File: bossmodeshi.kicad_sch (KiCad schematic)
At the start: 102 parts, among them Q1 FZT853TA, Q2 PSMN3R7-100BSE, Q3 PSMN3R7-100BSE, Q4 PSMN3R7-100BSE, Q5 PSMN3R7-100BSE, U10 SQ1464EEH-T1_GE3, U11 MP2790DFP-0000-T, U5 SQ1464EEH-T1_GE3, U6 SQ1464EEH-T1_GE3, U7 SQ1464EEH-T1_GE3, U8 SQ1464EEH-T1_GE3, U9 SQ1464EEH-T1_GE3

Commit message: Pushing
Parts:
- added D12, D18, D19, D20, D21, D22, D25: LED, symbol Device:LED
- added NT1: NetTie_2, NetTie:NetTie-2_SMD_Pad2.0mm, symbol Device:NetTie_2
- added R28, R29, R30, R31, R32, R33, R38: R, symbol Device:R
- R19: now fitted
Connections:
- net C1: now also R_BAL_6.1, R33.1; no longer R_BAL_6.2
- net C2: now also R_BAL_5.1, R32.1; no longer R_BAL_5.2
- net C3: now also R_BAL_4.1, R31.1; no longer R_BAL_4.2
- net C4: now also R_BAL_3.1, R30.1; no longer R_BAL_3.2
- net C5: now also R_BAL_2.1, R29.1; no longer R_BAL_2.2
- net GND: now also D25.1 (K), NT1.1; no longer D9.2 (A), DAGND_CO1.2 (A), R_CELL_FLT7.2, R_SENSE1.1, R_SRP_FLT1.1, U10.4 (S)
- net INT_5V: now also R38.2
- net TOP: now also R28.1
- net at U10.1 (D), U10.2 (D), U10.5 (D)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: now also R_BAL_6.2, D22.1 (K); no longer R_BAL_6.1
- net at U9.1 (D), U9.2 (D), U9.5 (D)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: now also R_BAL_5.2, D21.1 (K); no longer R_BAL_5.1
- net at U8.1 (D), U8.2 (D), U8.5 (D)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: now also R_BAL_4.2, D20.1 (K); no longer R_BAL_4.1
- net at U6.1 (D), U6.2 (D), U6.5 (D)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: now also R_BAL_2.2, D18.1 (K); no longer R_BAL_2.1
- net at U7.1 (D), U7.2 (D), U7.5 (D)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: now also R_BAL_3.2, D19.1 (K); no longer R_BAL_3.1
- net at R_BAL_1.1, U5.1 (D), U5.2 (D)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: now also D12.1 (K)
- new net: D20.2 (A), R31.2
- new net: D22.2 (A), R33.2
- new net: D21.2 (A), R32.2
- new net: D18.2 (A), R29.2
- new net: D25.2 (A), R38.1
- new net: D19.2 (A), R30.2
- new net: D12.2 (A), R28.2
- new net BATT-: D9.2 (A), DAGND_CO1.2 (A), NT1.2, R_CELL_FLT7.2, R_SENSE1.1, R_SRP_FLT1.1, U10.4 (S)
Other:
- note added: "One NTC to measure drain node."
- moved on the sheet: C19, C20, C21, C22, C23, C_3V3_1, C_CELL_FLT1, C_CELL_FLT2, C_CELL_FLT3, C_CELL_FLT4, C_CELL_FLT5, C_CELL_FLT6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

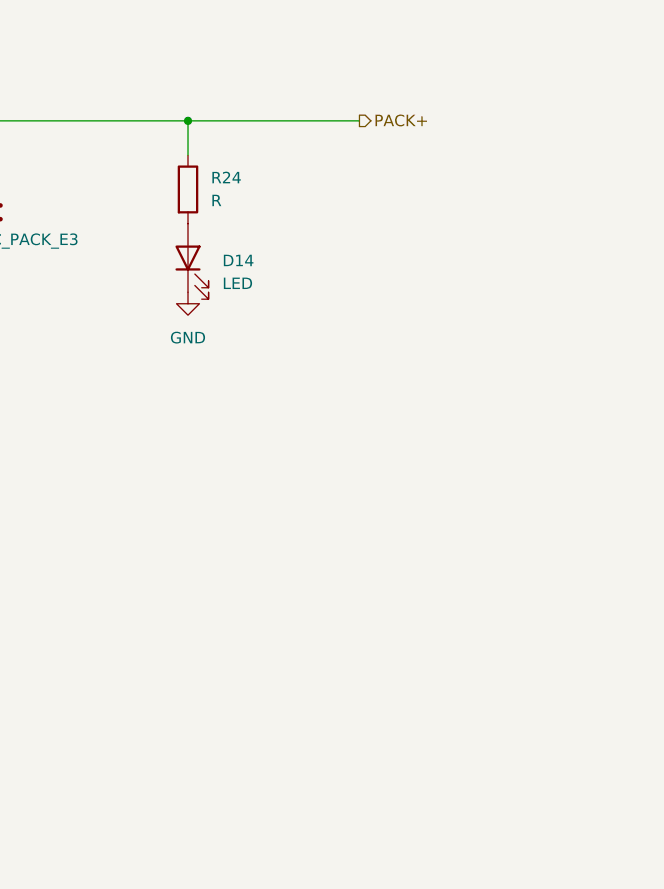
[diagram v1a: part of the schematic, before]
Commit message: reverse polarity protection
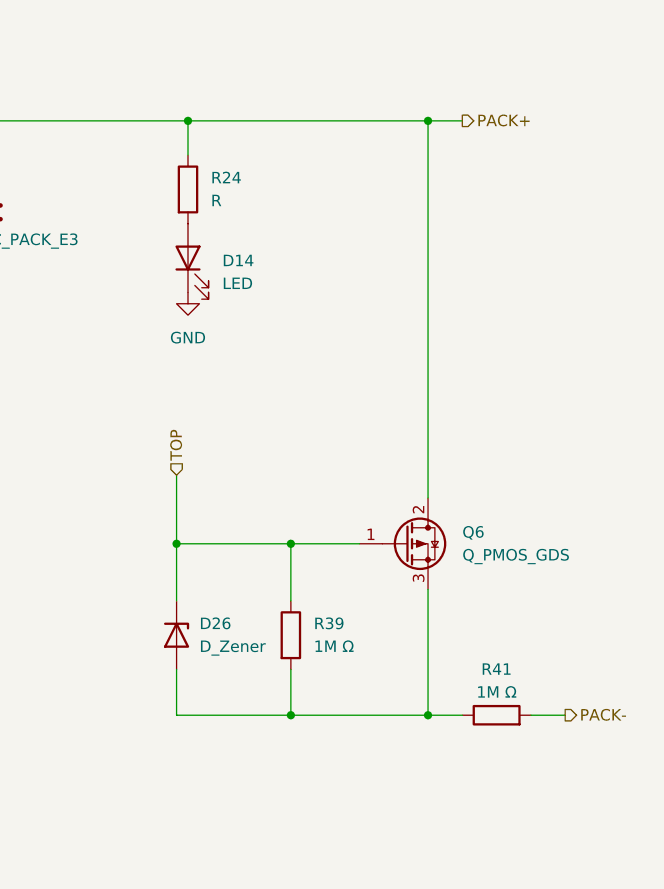
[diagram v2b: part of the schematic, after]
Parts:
- added D26: D_Zener, symbol Device:D_Zener
- added Q6: Q_PMOS_GDS, Package_TO_SOT_SMD:TO-252-2, symbol Transistor_FET:Q_PMOS_GDS
- added R39, R41: 1M Ω, Resistor_SMD:R_0201_0603Metric, symbol Device:R
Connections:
- net PACK+: now also Q6.2 (D)
- net PACK-: now also R41.2
- net TOP: now also D26.1 (K), Q6.1 (G), R39.1
- new net: D26.2 (A), Q6.3 (S), R39.2, R41.1

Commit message: Adding in signals and cleaning up schematic
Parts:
- removed D18, D19, D20, D21, D25: LED, symbol Device:LED
- removed R23: R, Resistor_SMD:R_0603_1608Metric, symbol Device:R
- removed R30, R31, R32, R33, R38: R, symbol Device:R
- added D11, D12, D15, D24, D27: LED, LED_SMD:LED_0603_1608Metric, symbol Device:LED
- added R25, R26, R27, R28, R37, R39: R, Resistor_SMD:R_0603_1608Metric, symbol Device:R
- added R42, R43, R44, R45, R46, R47, R48, R49: R, symbol Device:R
- D10: renamed from D12; footprint (none) -> LED_SMD:LED_0603_1608Metric
- D22: footprint (none) -> LED_SMD:LED_0603_1608Metric
- D26: value D_Zener -> TPSMF4L16A; footprint (none) -> Diode_SMD:Nexperia_CFP3_SOD-123W; Mfr (none) -> Littelfuse Inc.; Mfr P/N (none) -> TPSMF4L16A; Supplier_1 (none) -> Digikey; Supplier_1 P/N (none) -> F7539TR-ND; Supplier_1 Price @ QTY (none) -> 1; Supplier_1 Unit Price (none) -> 0.15000
- Q6: footprint Package_TO_SOT_SMD:TO-252-2 -> _BMS:SOT-23; Mfr P/N (none) -> SI01P10-TP; Mfr PN IRFR9110TRPBF -> (none); Supplier JLCPCB -> (none); Supplier PN C143721 -> (none); Supplier_2 (none) -> JLCPCB; Supplier_2 P/N (none) -> C5917586; Supplier_2 Price @ Qty (none) -> 1; Supplier_2 Unit Price (none) -> 0.0751
- R23: renamed from R28; footprint (none) -> Resistor_SMD:R_0603_1608Metric
- R29: footprint (none) -> Resistor_SMD:R_0603_1608Metric
- R40: renamed from R39; value 1M Ω -> 1MΩ; Mfr P/N (none) -> RC0603FR-071ML; Mfr PN RC0603FR-071ML -> (none); Supplier_2 (none) -> JLCPCB
- R41: value 1M Ω -> 1MΩ; Mfr P/N (none) -> RC0603FR-071ML; Mfr PN RC0603FR-071ML -> (none); Supplier_2 (none) -> JLCPCB
- renumbered C19 to C20, C20 to C21, C21 to C22, C22 to C23, C23 to C24, D4 to D16, D5 to D17, D6 to D18, D7 to D19, D8 to D20, D9 to D21, D10 to D23, D11 to D25, R14 to R30, R15 to R31, R16 to R32, R17 to R33, R18 to R34, R19 to R35, R20 to R36, R21 to R38, U9 to U10, U10 to U11, U11 to U12, U5 to U6, U6 to U7, U7 to U8, U8 to U9
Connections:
- net C1: now also R28.1
- net C2: now also R27.1
- net C3: now also R26.1
- net C4: now also R25.1
- net C5: now also R24.1; no longer R29.1
- net GND: now also D22.1 (K), D24.1 (K), D27.1 (K), R43.2, R45.2, R47.2, R49.2; no longer D13.1 (K), D14.1 (K)
- net INT_5V: now also R37.1
- net PACK+: now also R39.1, R42.1; no longer R24.1
- net TOP: now also R29.1, R44.1; no longer D26.1 (K), Q6.1 (G), R40.1
- net CHG_M: now reaches D_CHG_VGS1.1 (K), R_CHG_DRIVER1.2, R_CHG_MG1.2, R_CHG_MG2.1, R_CHG_PUP1.2
- net CHG_M: now also R48.1
- net at D26.2 (A), R40.2, R41.1: now also Q6.1 (G); no longer Q6.3 (S)
- net at R_BAL_6.2, U11.1 (D), U11.2 (D)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: now also D15.1 (K); no longer D22.1 (K)
- net DSG_M: now reaches D_CHG_VGS2.1 (K), R_DSG_DRIVER1.1, R_DSG_MG1.2, R_DSG_MG2.1, R_DSG_PUP1.1
- net DSG_M: now also R46.1
- net at R_BAL_5.2, U10.1 (D), U10.2 (D)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: now also D14.1 (K)
- net at D22.2 (A): now also R29.2
- net at R_BAL_4.2, U9.1 (D), U9.2 (D)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: now also D13.1 (K)
- net at R_BAL_2.2, U7.1 (D), U7.2 (D)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: now also D11.1 (K)
- net at R_BAL_3.2, U8.1 (D), U8.2 (D)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: now also D12.1 (K)
- net at D13.2 (A): now also R26.2
- net at R24.2: now also D11.2 (A); no longer D14.2 (A)
- new net: D24.2 (A), R37.2
- new net: D15.2 (A), R28.2
- new net: D14.2 (A), R27.2
- new net: D27.2 (A), R39.2
- new net: D12.2 (A), R25.2
- new net CHG_MV: R48.2, R49.1
- new net DSG_MV: R46.2, R47.1
- new net PACKV: R42.2, R43.1
- new net PACK_F: D26.1 (K), Q6.3 (S), R40.1
- new net TOPV: R44.2, R45.1
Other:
- note added: "Pack voltage divider"
- note added: "Reverse polarity protection"
- note added: "Signals & Comms"
- moved on the sheet: Q6, R40

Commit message: Redoing layout
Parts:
- removed D10, D11, D12, D13, D14, D15: LED, LED_SMD:LED_0603_1608Metric, symbol Device:LED
- removed R23, R24, R25, R26, R27, R28: R, Resistor_SMD:R_0603_1608Metric, symbol Device:R
- R40, R41: footprint Resistor_SMD:R_0201_0603Metric -> Resistor_SMD:R_0603_1608Metric
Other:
- moved on the sheet: R_BAL_1, R_BAL_2, R_BAL_3, R_BAL_4, R_BAL_5, R_BAL_6

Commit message: prepaing for production
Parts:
- added R36, R37, R38, R39, R40, R41: 10k, Resistor_SMD:R_0603_1608Metric, symbol Device:R
- added TP11, TP12, TP13, TP14: TestPoint, _BMS:Harwin TP, symbol Connector:TestPoint
- C_3V3_1, C_REG1, C_VDD1: Supplier_2 (none) -> JLCPCB; Supplier_2 P/N (none) -> C22443289
- C_CP1: Mfr P/N CC0402JRX7R9BB473 -> CC0603JRX7R9BB473; Supplier_1 DigiKey -> (none); Supplier_1 P/N 13-CC0402JRX7R9BB473TR-ND -> (none); Supplier_1 Price @ QTY 1 -> (none); Supplier_1 Unit Price 0.10000 -> (none); Supplier_2 (none) -> JLCPCB; Supplier_2 P/N (none) -> C519554
- C_MID1: Mfr Murata Electronics -> YAGEO; Mfr P/N GRM155C71H104JE19D -> CC0603JRX7R9BB104; Supplier_1 DigiKey -> (none); Supplier_1 P/N 490-GRM155C71H104JE19DTR-ND -> (none); Supplier_1 Price @ QTY 1 -> (none); Supplier_1 Unit Price 0.10000 -> (none); Supplier_2 (none) -> JLCPCB; Supplier_2 P/N (none) -> C91183
- C_PACK_E1, C_PACK_E2: now left out of the parts list
- C_PACK_E3: now not fitted; now left out of the parts list
- C_REGIN1: Mfr Cal-Chip Electronics, Inc. -> TDK; Mfr P/N GMC10X5R335K25NT -> C1608X5R1E335KT000E; Supplier_1 DigiKey -> (none); Supplier_1 P/N 4713-GMC10X5R335K25NTTR-ND -> (none); Supplier_1 Price @ QTY 0.41000 -> (none); Supplier_1 Unit Price 1 -> (none); Supplier_2 (none) -> JLCPCB; Supplier_2 P/N (none) -> C342962
- C_TOP_FLT1: Mfr TDK Corporation -> YAGEO; Mfr P/N CGA3E3X7R1H474K080AE -> CC0603KRX7R9BB474; Supplier_1 Digikey -> (none); Supplier_1 P/N 445-172475-2-ND -> (none); Supplier_1 Price @ QTY 1 -> (none); Supplier_1 Unit Price 0.31000 -> (none); Supplier_2 (none) -> JLCPCB; Supplier_2 P/N (none) -> C513577; Supplier_2 Price @ QTY (none) -> 0.0105; Supplier_2 Unit Price (none) -> 1
- C_VREF1: Supplier_2 (none) -> JLCPCB; Supplier_2 P/N (none) -> C22443289; Supplier_2 Price @ QTY (none) -> 1; Supplier_2 Unit Price (none) -> 0.0703
- D10: renamed from D16; Supplier_2 (none) -> JLCPCB; Supplier_2 P/N (none) -> C478011
- D11: renamed from D17; Supplier_2 (none) -> JLCPCB; Supplier_2 P/N (none) -> C478011
- D12: renamed from D18; Supplier_2 (none) -> JLCPCB; Supplier_2 P/N (none) -> C478011
- D13: renamed from D19; Supplier_2 (none) -> JLCPCB; Supplier_2 P/N (none) -> C478011
- D14: renamed from D20; Supplier_2 (none) -> JLCPCB; Supplier_2 P/N (none) -> C478011
- D15: renamed from D21; Supplier_2 (none) -> JLCPCB; Supplier_2 P/N (none) -> C478011
- D16: renamed from D22; Mfr (none) -> ROHM Semicon; Mfr P/N (none) -> SML-310LTT86; Supplier_2 (none) -> JLCPCB; Supplier_2 P/N (none) -> C79636
- D17: renamed from D23; Supplier_2 (none) -> JLCPCB
- D18: renamed from D24; Mfr (none) -> ROHM Semicon; Mfr P/N (none) -> SML-E12P8WT86; Supplier_2 (none) -> JLCPCB; Supplier_2 P/N (none) -> C126319
- D19: renamed from D25; Supplier_2 (none) -> JLCPCB; Supplier_2 P/N (none) -> C5557780
- D20: renamed from D26; Supplier_2 (none) -> JLCPCB; Supplier_2 P/N (none) -> C468927
- D21: renamed from D27; Mfr (none) -> ROHM Semicon; Mfr P/N (none) -> SML-310LTT86; Supplier_2 (none) -> JLCPCB; Supplier_2 P/N (none) -> C79636
- DAGND_CO1: Supplier_2 (none) -> JLCPCB; Supplier_2 P/N (none) -> C150503
- D_CHG_VGS1, D_CHG_VGS2: Supplier_2 (none) -> JLCPCB; Supplier_2 P/N (none) -> C468927
- Q1: Supplier_2 (none) -> JLCPCB; Supplier_2 P/N (none) -> C435890
- Q2, Q3, Q4, Q5: Supplier_2 (none) -> JLCPCB; Supplier_2 P/N (none) -> C406802
- R23: renamed from R29; value R -> 10k; Mfr (none) -> YAGEO; Mfr P/N (none) -> RC0603FR-0710KL; Supplier_2 (none) -> JLCPCB; Supplier_2 P/N (none) -> C98220
- R26: renamed from R32; now left out of the parts list
- R27: renamed from R33; now left out of the parts list
- R28: renamed from R34; now left out of the parts list
- R29: renamed from R35; symbol Device:R -> Device:Thermistor_NTC; Mfr (none) -> Vishay Intertech; Mfr P/N (none) -> NTCS0603E3103FLT; Supplier_2 (none) -> JLCPCB; Supplier_2 P/N (none) -> C142556
- R31: renamed from R37; Mfr (none) -> Yageo; Mfr P/N (none) -> AC0603FR-071KL; Supplier_2 (none) -> JLCPCB; Supplier_2 P/N (none) -> C116692
- R33: renamed from R40; Supplier_2 P/N (none) -> C105578
- R34: renamed from R39; value R -> 10k; Mfr (none) -> YAGEO; Mfr P/N (none) -> RC0603FR-0710KL; Supplier_2 (none) -> JLCPCB; Supplier_2 P/N (none) -> C98220
- R35: renamed from R41; Supplier_2 P/N (none) -> C105578
- R42, R43: value R -> 10k; footprint (none) -> Resistor_SMD:R_0603_1608Metric; Mfr (none) -> Yageo; Mfr P/N (none) -> RC0603FR-0710KL; Supplier_2 (none) -> JLCPCB; Supplier_2 P/N (none) -> C98220; now not fitted; now left out of the parts list
- R44, R45, R46, R47, R48, R49: value R -> 10k; footprint (none) -> Resistor_SMD:R_0603_1608Metric; Mfr (none) -> YAGEO; Mfr P/N (none) -> RC0603FR-0710KL; Supplier_2 (none) -> JLCPCB; Supplier_2 P/N (none) -> C98220; now not fitted; now left out of the parts list
- R_BAL_1, R_BAL_2, R_BAL_3, R_BAL_4, R_BAL_5, R_BAL_6: Mfr YAGEO -> Vishay Intertech; Mfr P/N AC1206FR-7W43RL -> CRCW120643R0FKEAHP; Supplier_1 Digikey -> (none); Supplier_1 P/N 13-AC1206FR-7W43RLTR-ND -> (none); Supplier_1 Price @ QTY 1 -> (none); Supplier_1 Unit Price 0.13000 -> (none); Supplier_2 (none) -> JLCPCB; Supplier_2 P/N (none) -> C4017025
- R_CHG_PUP1, R_DSG_PUP1: Supplier_2 (none) -> JLCPCB; Supplier_2 P/N (none) -> C159944
- R_MID1, R_PACK_FLT1: Supplier_2 P/N C844725 -> C844725
- R_REG1: Mfr Vishay Dale Thin Film -> Vishay Intertech; Mfr P/N PTN1206Y5000BST1 -> TNPW1206100RBEEA; Supplier_1 DigiKey -> (none); Supplier_1 P/N 764-PTN1206Y5000BST1TR-ND -> (none); Supplier_1 Price @ QTY 1 -> (none); Supplier_1 Unit Price 0.86420 -> (none); Supplier_2 (none) -> JLCPCB; Supplier_2 P/N (none) -> C844470
- R_SENSE1: Mfr P/N PA2512DKF7W0R002E -> PA2512FKE7W0R002E; Supplier_1 DigiKey -> (none); Supplier_1 P/N 13-PA2512DKF7W0R002ETR-ND -> (none); Supplier_1 Price @ QTY 1 -> (none); Supplier_1 Unit Price 1.59000 -> (none); Supplier_2 (none) -> JLCPCB; Supplier_2 P/N (none) -> C728306
- R_TOP_FLT1: value 20 Ω -> 100; Mfr P/N AT0402BRD0720RL -> CRCW0603100RFKEAHP; Supplier_1 DigiKey -> (none); Supplier_1 P/N 541-10438-2-ND -> (none); Supplier_1 Price @ QTY 0.13634 -> (none); Supplier_1 Unit Price 1 -> (none); Supplier_2 (none) -> JLCPCB; Supplier_2 P/N (none) -> C844725
- TP10, TP4, TP5, TP6, TP7, TP8, TP9: Mfr (none) -> Harwin; Mfr P/N (none) -> S2761-46R; Supplier_2 (none) -> JLCPCB; Supplier_2 P/N (none) -> C5846954
- U10: renamed from U11; Supplier_2 (none) -> JLCPCB; Supplier_2 P/N (none) -> C5900582
- U11: renamed from U12; Supplier_2 (none) -> JLCPCB; Supplier_2 P/N (none) -> C23282104
- U5: renamed from U6; Supplier_2 (none) -> JLCPCB; Supplier_2 P/N (none) -> C5900582
- U6: renamed from U7; Supplier_2 (none) -> JLCPCB; Supplier_2 P/N (none) -> C5900582
- U7: renamed from U8; Supplier_2 (none) -> JLCPCB; Supplier_2 P/N (none) -> C5900582
- U8: renamed from U9; Supplier_2 (none) -> JLCPCB; Supplier_2 P/N (none) -> C5900582
- U9: renamed from U10; Supplier_2 (none) -> JLCPCB; Supplier_2 P/N (none) -> C5900582
- renumbered R30 to R24, R31 to R25, R36 to R30, R38 to R32
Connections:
- net C10 is gone; now on net CELL_6: U11.46 (C10), U11.47 (C10), U11.48 (C10)
- net CELL_0: now also R49.2
- net CELL_1: now also R48.2, R49.1
- net CELL_2: now also R47.2, R48.1
- net CELL_3: now also R46.2, R47.1
- net CELL_4: now also R44.2, R46.1
- net CELL_5: now also R44.1, R45.2
- net CELL_6: now also R45.1
- net CHG_M: now also R42.1; no longer R48.1
- net CHG_MV: now also R42.2, R43.1; no longer R48.2, R49.1
- net DRAIN: now also TP13.1
- net DSG_M: now also R40.1; no longer R46.1
- net DSG_MV: now also R40.2, R41.1; no longer R46.2, R47.1
- net GND: now also R37.2, R39.2, R41.2; no longer R45.2, R47.2, R49.2
- net PACK+: now also R36.1, TP11.1; no longer R42.1, R_PACK_FLT1.2
- net PACKV: now also R36.2, R37.1; no longer R42.2, R43.1
- net PACK_F: now also R_PACK_FLT1.2, TP14.1
- net TOP: now also R38.1, TP12.1; no longer R44.1
- net TOPV: now also R38.2, R39.1; no longer R44.2, R45.1
- net GPIO2: now reaches U11.35 (GPIO2)
- net GPIO1: now reaches U11.36 (GPIO1)
- no-connect marks 6 -> 4
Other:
- note added: "Resistors are meant to simulate a cells. Voltage divider."
- note added: "Using IRFS7734TRLPBF FETs, NOT PSMN3R7-BSEJ"

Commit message: Fixes
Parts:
- R31: value R -> 1k
- R_CHG_PUP1, R_DSG_PUP1: Mfr KOA Speer Electronics, Inc. -> UNI-ROYAL(Uniroyal Elec); Mfr P/N RK73H1ETTP1005F -> 0603WAF1005T5E; Supplier_1 Digikey -> (none); Supplier_1 P/N 2019-RK73H1ETTP1005FTR-ND -> (none); Supplier_1 Price @ QTY 1 -> (none); Supplier_1 Unit Price 0.10000 -> (none); Supplier_2 P/N C159944 -> C7250
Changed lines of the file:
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@@
 			)
 		)
-		(property "Value" "R"
+		(property "Value" "1k"
 			(at 269.24 271.7799 0)
 			(effects
@@
 			)
 		)
-		(property "Description" "RES 10M OHM 1% 1/10W 0402"
+		(property "Description" "100mW 10MΩ 75V Thick Film Resistor ±1% ±100ppm/℃ 0603"
 			(at 341.63 101.6 0)
 			(effects
@@
 			)
 		)
-		(property "Mfr" "KOA Speer Electronics, Inc."
+		(property "Mfr" "UNI-ROYAL(Uniroyal Elec)"
 			(at 341.63 101.6 0)
 			(effects
@@
 			)
 		)
-		(property "Mfr P/N" "RK73H1ETTP1005F"
+		(property "Mfr P/N" "0603WAF1005T5E"
 			(at 341.63 101.6 0)
 			(effects
@@
 			)
 		)
-		(property "Supplier_1" "Digikey"
+		(property "Supplier_1" ""
 			(at 341.63 101.6 90)
 			(effects
@@
 			)
 		)
-		(property "Supplier_1 P/N" "2019-RK73H1ETTP1005FTR-ND"
+		(property "Supplier_1 P/N" ""
 			(at 341.63 101.6 90)
 			(effects
@@
 			)
 		)
-		(property "Supplier_1 Price @ QTY" "1"
+		(property "Supplier_1 Price @ QTY" ""
 			(at 341.63 101.6 90)
 			(effects
@@
 			)
 		)
-		(property "Supplier_1 Unit Price" "0.10000"
+		(property "Supplier_1 Unit Price" ""
 			(at 341.63 101.6 90)
 			(effects
@@
 			)
 		)
-		(property "Supplier_2 P/N" "C159944"
+		(property "Supplier_2 P/N" "C7250"
 			(at 341.63 101.6 90)
 			(effects
@@
 			)
 		)
-		(property "Description" "RES 10M OHM 1% 1/10W 0402"
+		(property "Description" "100mW 10MΩ 75V Thick Film Resistor ±1% ±100ppm/℃ 0603"
 			(at 288.29 101.6 0)
 			(effects
@@
 			)
 		)
-		(property "Mfr" "KOA Speer Electronics, Inc."
+		(property "Mfr" "UNI-ROYAL(Uniroyal Elec)"
 			(at 288.29 101.6 0)
 			(effects
@@
 			)
 		)
-		(property "Mfr P/N" "RK73H1ETTP1005F"
+		(property "Mfr P/N" "0603WAF1005T5E"
 			(at 288.29 101.6 0)
 			(effects
@@
 			)
 		)
-		(property "Supplier_1" "Digikey"
+		(property "Supplier_1" ""
 			(at 288.29 101.6 90)
 			(effects
@@
 			)
 		)
-		(property "Supplier_1 P/N" "2019-RK73H1ETTP1005FTR-ND"
+		(property "Supplier_1 P/N" ""
 			(at 288.29 101.6 90)
 			(effects
@@
 			)
 		)
-		(property "Supplier_1 Price @ QTY" "1"
+		(property "Supplier_1 Price @ QTY" ""
 			(at 288.29 101.6 90)
 			(effects
@@
 			)
 		)
-		(property "Supplier_1 Unit Price" "0.10000"
+		(property "Supplier_1 Unit Price" ""
 			(at 288.29 101.6 90)
 			(effects
@@
 			)
 		)
-		(property "Supplier_2 P/N" "C159944"
+		(property "Supplier_2 P/N" "C7250"
 			(at 288.29 101.6 90)
 			(effects
